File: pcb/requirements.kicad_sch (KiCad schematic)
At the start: 10 parts

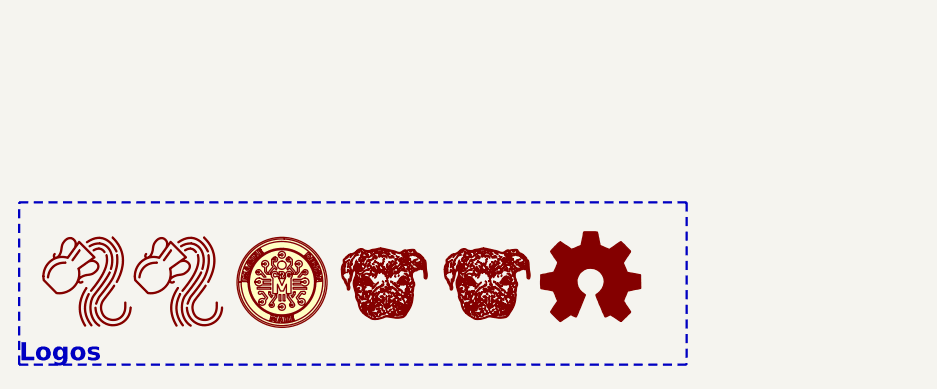
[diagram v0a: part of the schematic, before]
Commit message: Fixed sillkscreen and renders
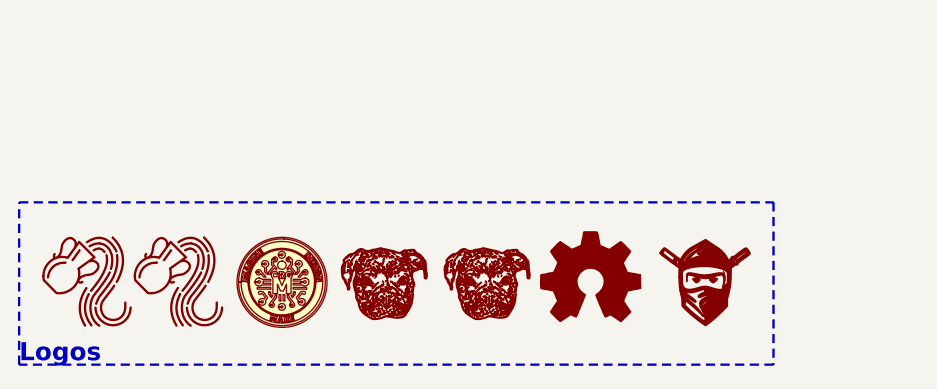
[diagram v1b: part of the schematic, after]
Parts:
- added LOGO7: ~, CRGM Logos:FNWW Face 5mm, symbol CRGM Logos:FNWW Face
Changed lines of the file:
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@@
 	(rectangle
 		(start 15.24 177.8)
-		(end 89.408 195.834)
+		(end 99.06 195.834)
 		(stroke
 			(width 0.254)
@@
 					(unit 1)
 				)
+			)
+		)
+	)
+	(symbol
+		(lib_id "CRGM Logos:FNWW Face")
+		(at 91.44 186.69 0)
+		(unit 1)
+		(exclude_from_sim no)
+		(in_bom yes)
+		(on_board yes)
+		(dnp no)
+		(property "Reference" "LOGO7"
+			(at 91.44 193.548 0)
+			(effects
+				(font
+					(size 1.27 1.27)
+				)
+				(hide yes)
+			)
+		)
+		(property "Value" "~"
+			(at 88.9 181.864 0)
+			(effects
+				(font
+					(size 1.27 1.27)
+				)
+				(hide yes)
+			)
+		)
+		(property "Footprint" "CRGM Logos:FNWW Face 5mm"
+			(at 91.44 195.834 0)
+			(effects
+				(font
+					(size 1.27 1.27)
+				)
+				(hide yes)
+			)
+		)
+		(property "Datasheet" ""
+			(at 88.9 181.864 0)
+			(effects
+				(font
+					(size 1.27 1.27)
+				)
+				(hide yes)
+			)
+		)
+		(property "Description" ""
+			(at 88.9 181.864 0)
+			(effects
+				(font
+					(size 1.27 1.27)
+				)
+				(hide yes)
+			)
+		)
+		(property "LCSC" ""
+			(at 91.44 186.69 0)
+			(effects
+				(font
+					(size 1.27 1.27)
+				)
+				(hide yes)
+			)
+		)
+		(property "Digikey" ""
+			(at 91.44 186.69 0)
+			(effects
+				(font
+					(size 1.27 1.27)
+				)
+				(hide yes)
+			)
+		)
+		(property "Mouser" ""
+			(at 91.44 186.69 0)
+			(effects
+				(font
+					(size 1.27 1.27)
+				)
+				(hide yes)
+			)
+		)
+		(instances
+			(project ""
+				(path "/a8149920-3b7f-4d7d-8e96-7a0b38870225/286c1f37-b285-4c3f-bd6d-061a220fab98"
+					(reference "LOGO7")
+					(unit 1)
+				)

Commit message: Changed I2C to open instead of bridged
Moved I2C jumper to back
Changed to open instead of bridged
Changed Roxy to 5mm on front
Moved silkscreen around.
Updated renders
Removed logos from BOM
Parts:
- LOGO5: footprint CRGM Logos:Roxy 3.5mm -> CRGM Logos:Roxy 5mm
- LOGO7: now left out of the parts list
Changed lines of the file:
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@@
 			)
 		)
-		(property "Footprint" "CRGM Logos:Roxy 3.5mm"
+		(property "Footprint" "CRGM Logos:Roxy 5mm"
 			(at 67.31 194.818 0)
 			(effects
@@
 		(unit 1)
 		(exclude_from_sim no)
-		(in_bom yes)
+		(in_bom no)
 		(on_board yes)
 		(dnp no)

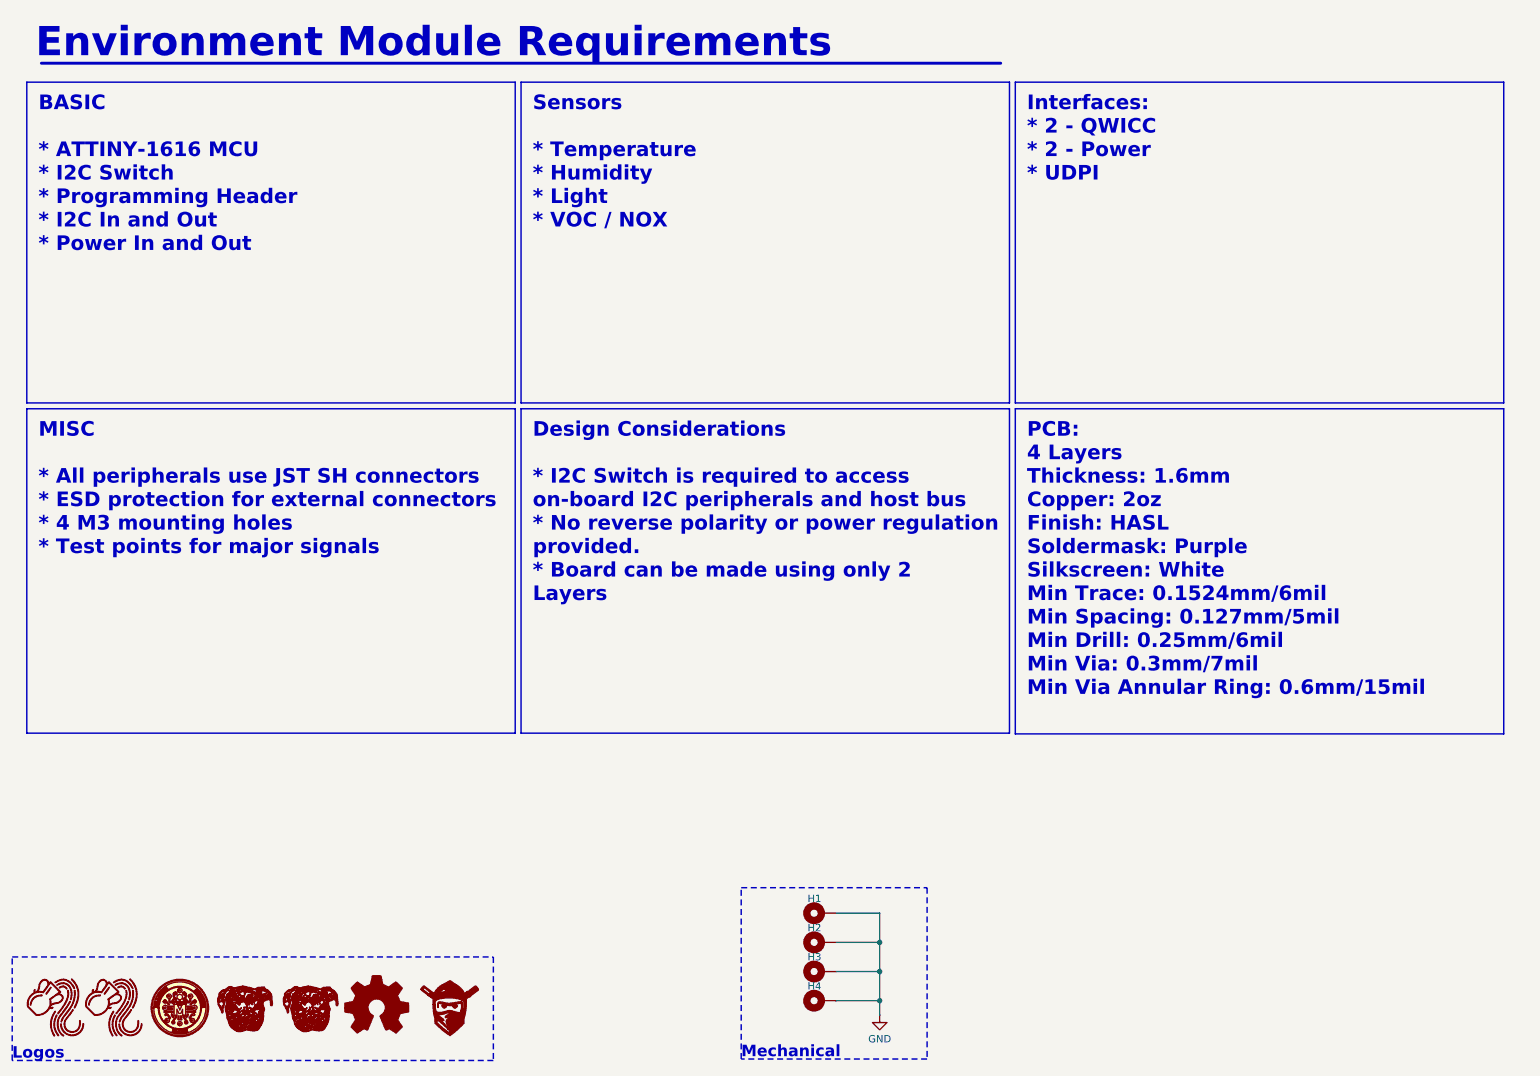
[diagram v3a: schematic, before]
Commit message: Redesign with cutouts for sensors
Removed power connectors since 5V is not needed
Added cutout for VOC sensor
Rerouted sensor section
Rescaled logos and fixed silkscreen
Changed to blue LED for power indicator
Updated requirements and renders
Changed all 0.1uF caps to small symbol
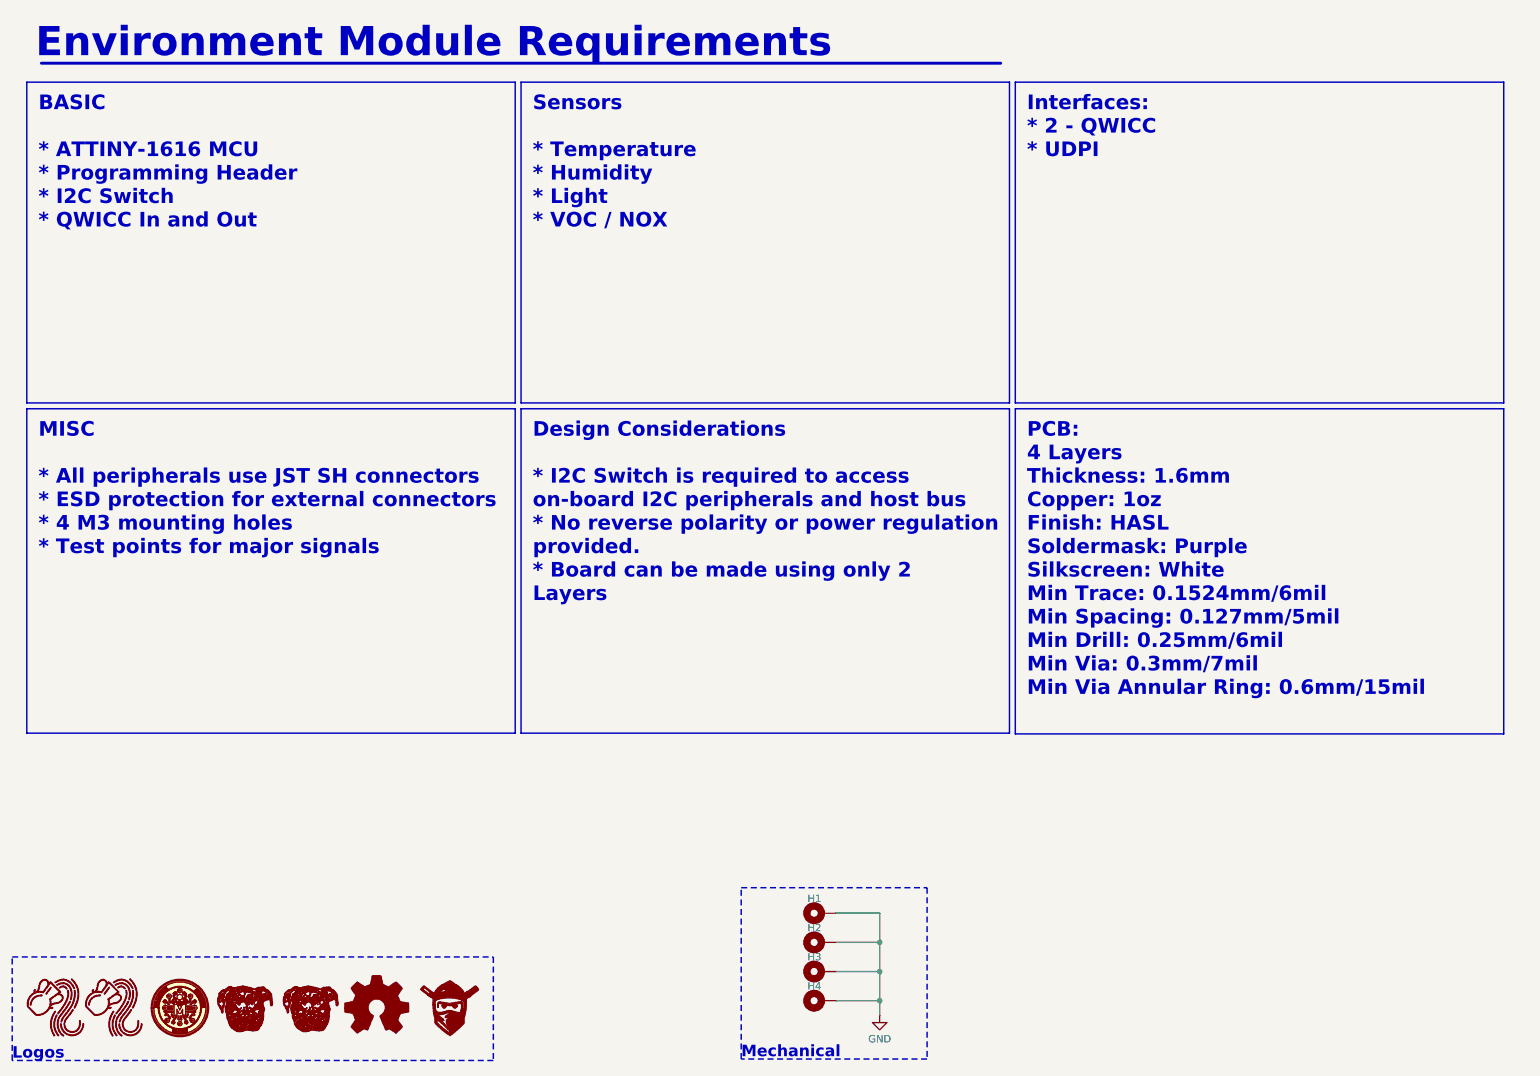
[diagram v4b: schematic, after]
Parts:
- LOGO5: footprint CRGM Logos:Roxy 5mm -> CRGM Logos:Roxy 4mm
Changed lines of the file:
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@@
 		)
 	)
-	(text_box "Interfaces:\n* 2 - QWICC\n* 2 - Power\n* UDPI"
+	(text_box "Interfaces:\n* 2 - QWICC\n* UDPI"
 		(exclude_from_sim yes)
 		(at 189.992 25.4 0)
@@
 		)
 	)
-	(text_box "PCB:\n4 Layers\nThickness: 1.6mm\nCopper: 2oz\nFinish: HASL\nSoldermask: Purple\nSilkscreen: White\nMin Trace: 0.1524mm/6mil\nMin Spacing: 0.127mm/5mil\nMin Drill: 0.25mm/6mil\nMin Via: 0.3mm/7mil\nMin Via Annular Ring: 0.6mm/15mil\n\n"
+	(text_box "PCB:\n4 Layers\nThickness: 1.6mm\nCopper: 1oz\nFinish: HASL\nSoldermask: Purple\nSilkscreen: White\nMin Trace: 0.1524mm/6mil\nMin Spacing: 0.127mm/5mil\nMin Drill: 0.25mm/6mil\nMin Via: 0.3mm/7mil\nMin Via Annular Ring: 0.6mm/15mil\n\n"
 		(exclude_from_sim yes)
 		(at 189.992 82.296 0)
@@
 		)
 	)
-	(text_box "BASIC\n\n* ATTINY-1616 MCU\n* I2C Switch\n* Programming Header\n* I2C In and Out\n* Power In and Out\n\n"
+	(text_box "BASIC\n\n* ATTINY-1616 MCU\n* Programming Header\n* I2C Switch\n* QWICC In and Out\n\n"
 		(exclude_from_sim yes)
 		(at 17.78 25.4 0)
@@
 			)
 		)
-		(property "Footprint" "CRGM Logos:Roxy 5mm"
+		(property "Footprint" "CRGM Logos:Roxy 4mm"
 			(at 67.31 194.818 0)
 			(effects

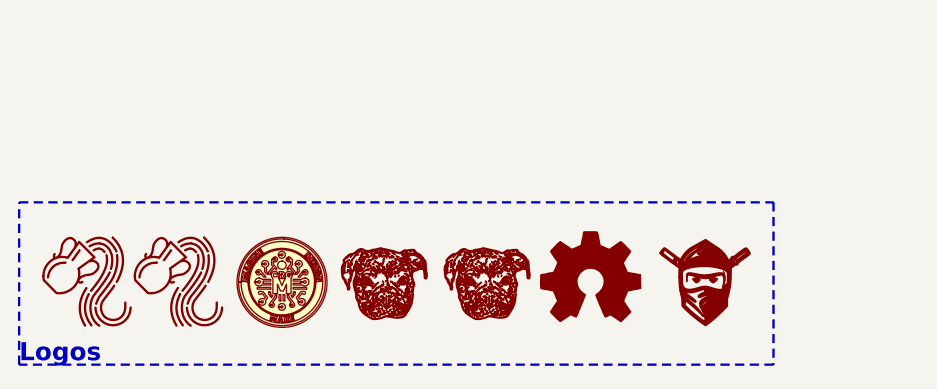
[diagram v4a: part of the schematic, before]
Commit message: Removed FNWW logo
Adjusted silkscreen on back
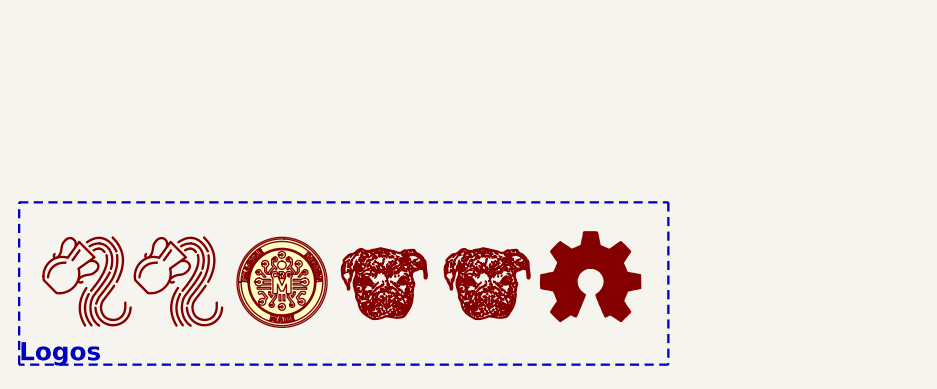
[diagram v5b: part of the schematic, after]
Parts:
- removed LOGO7: ~, CRGM Logos:FNWW Face 5mm, symbol CRGM Logos:FNWW Face
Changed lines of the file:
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@@
 	(rectangle
 		(start 15.24 177.8)
-		(end 99.06 195.834)
+		(end 87.376 195.834)
 		(stroke
 			(width 0.254)
@@
 					(unit 1)
 				)
-			)
-		)
-	)
-	(symbol
-		(lib_id "CRGM Logos:FNWW Face")
-		(at 91.44 186.69 0)
-		(unit 1)
-		(exclude_from_sim no)
-		(in_bom no)
-		(on_board yes)
-		(dnp no)
-		(property "Reference" "LOGO7"
-			(at 91.44 193.548 0)
-			(effects
-				(font
-					(size 1.27 1.27)
-				)
-				(hide yes)
-			)
-		)
-		(property "Value" "~"
-			(at 88.9 181.864 0)
-			(effects
-				(font
-					(size 1.27 1.27)
-				)
-				(hide yes)
-			)
-		)
-		(property "Footprint" "CRGM Logos:FNWW Face 5mm"
-			(at 91.44 195.834 0)
-			(effects
-				(font
-					(size 1.27 1.27)
-				)
-				(hide yes)
-			)
-		)
-		(property "Datasheet" ""
-			(at 88.9 181.864 0)
-			(effects
-				(font
-					(size 1.27 1.27)
-				)
-				(hide yes)
-			)
-		)
-		(property "Description" ""
-			(at 88.9 181.864 0)
-			(effects
-				(font
-					(size 1.27 1.27)
-				)
-				(hide yes)
-			)
-		)
-		(property "LCSC" ""
-			(at 91.44 186.69 0)
-			(effects
-				(font
-					(size 1.27 1.27)
-				)
-				(hide yes)
-			)
-		)
-		(property "Digikey" ""
-			(at 91.44 186.69 0)
-			(effects
-				(font
-					(size 1.27 1.27)
-				)
-				(hide yes)
-			)
-		)
-		(property "Mouser" ""
-			(at 91.44 186.69 0)
-			(effects
-				(font
-					(size 1.27 1.27)
-				)
-				(hide yes)
-			)
-		)
-		(instances
-			(project ""
-				(path "/a8149920-3b7f-4d7d-8e96-7a0b38870225/286c1f37-b285-4c3f-bd6d-061a220fab98"
-					(reference "LOGO7")
-					(unit 1)
-				)

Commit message: Changed to inside cutouts
Updated renders
Increased size of Roxy on front ❤️
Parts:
- LOGO5: footprint CRGM Logos:Roxy 4mm -> CRGM Logos:Roxy 6.5mm
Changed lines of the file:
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@@
 			)
 		)
-		(property "Footprint" "CRGM Logos:Roxy 4mm"
+		(property "Footprint" "CRGM Logos:Roxy 6.5mm"
 			(at 67.31 194.818 0)
 			(effects

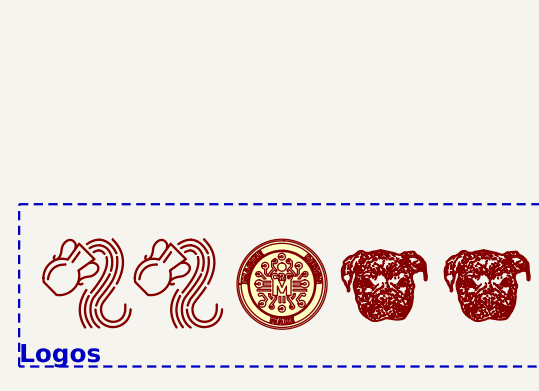
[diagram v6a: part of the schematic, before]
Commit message: Adjusted spacing and alignment of parts
Moved temp and voc to be on grid
Updated renders
Ran ERC -- fixed errors
Ran DRC -- fixed errors
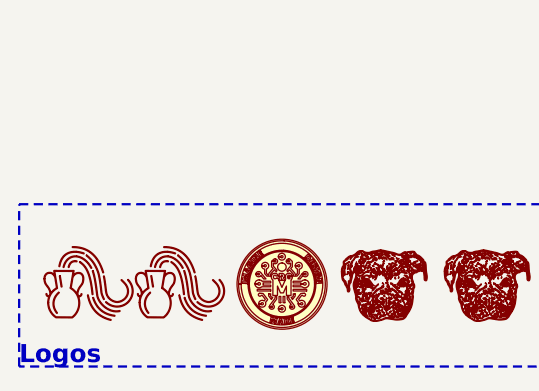
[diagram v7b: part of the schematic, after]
